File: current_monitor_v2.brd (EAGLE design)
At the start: 77.5 x 53.3 mm, 21 parts, among them IC1 LT1495, J1 1X2-3.5MM, J2 1X2-3.5MM, SW2 Display, T1 2N3904, T2 2N3904, U1 ARDUINO_SHIELDLABEL

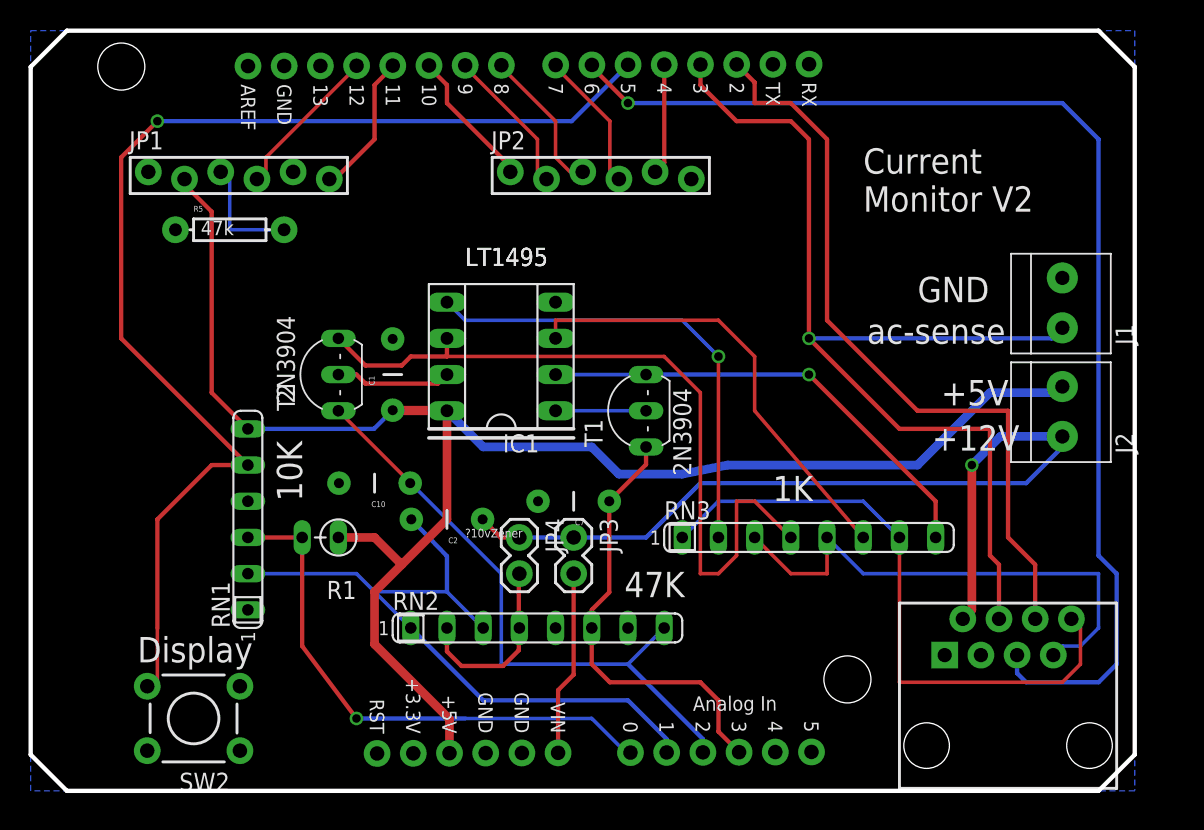
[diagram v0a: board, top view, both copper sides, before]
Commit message: changed v1.1 to v1-1 to please git, surface mount board ready to submit to osh park
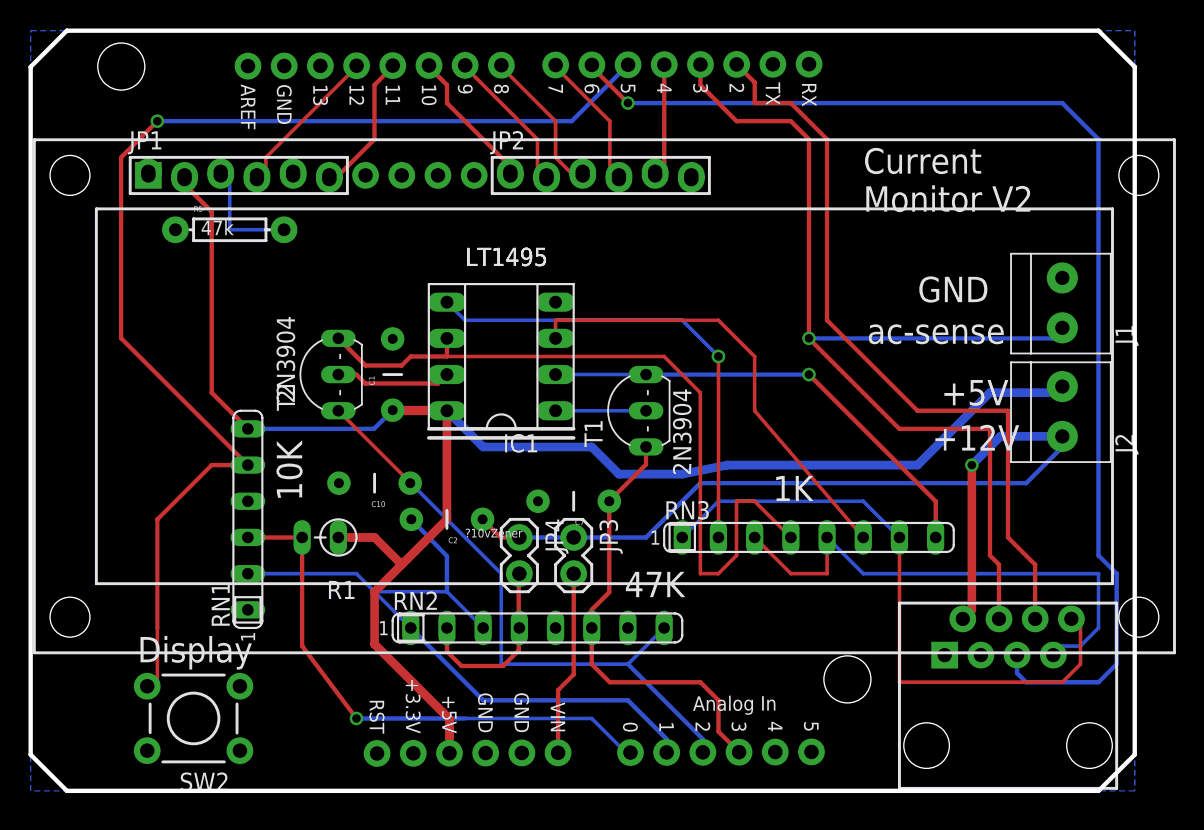
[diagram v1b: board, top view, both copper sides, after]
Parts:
- added U2: LCD-16X2SILK, SparkFun-Displays:LCD-16X2
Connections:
- new net A: U2.15
- new net K: U2.16
- new net VDD: U2.2
- new net VSS: U2.1
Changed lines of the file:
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@@
 <layer number="21" name="tPlace" color="7" fill="1" visible="yes" active="yes"/>
 <layer number="22" name="bPlace" color="7" fill="1" visible="no" active="yes"/>
-<layer number="23" name="tOrigins" color="15" fill="1" visible="no" active="yes"/>
+<layer number="23" name="tOrigins" color="15" fill="1" visible="yes" active="yes"/>
 <layer number="24" name="bOrigins" color="15" fill="1" visible="no" active="yes"/>
 <layer number="25" name="tNames" color="7" fill="1" visible="no" active="yes"/>
@@
 <element name="JP3" library="SparkFun-Passives" package="1X02" value="" x="38.1" y="17.78" rot="R270"/>
 <element name="JP4" library="SparkFun-Passives" package="1X02" value="" x="34.29" y="17.78" rot="R270"/>
+<element name="U2" library="SparkFun-Displays" package="LCD-16X2" value="LCD-16X2SILK" x="40.259" y="27.686"/>
 </elements>
 <signals>
@@
 <wire x1="34.25" y1="15.2" x2="34.29" y2="15.24" width="0.3048" layer="1"/>
 </signal>
+<signal name="A">
+<contactref element="U2" pad="15"/>
+</signal>
+<signal name="K">
+<contactref element="U2" pad="16"/>
+</signal>
+<signal name="VDD">
+<contactref element="U2" pad="2"/>
+</signal>
+<signal name="VSS">
+<contactref element="U2" pad="1"/>
+</signal>
 </signals>
